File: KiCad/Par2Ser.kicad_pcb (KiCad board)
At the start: 2 copper layers, 47 x 50 mm, 31 parts, among them J1 DB25_Male, J2 USB_C_Receptacle_USB2.0, U1 LC4032V-5TN48C, U3 FT240XS-R

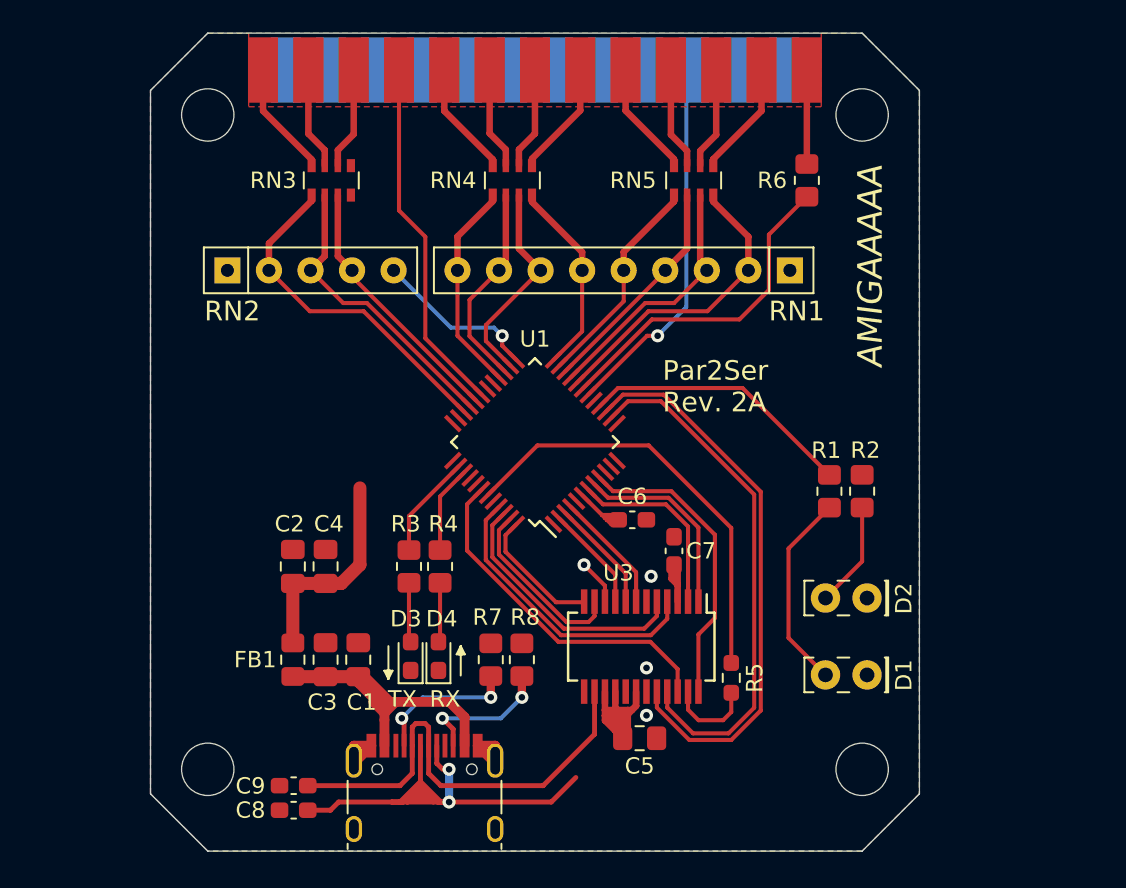
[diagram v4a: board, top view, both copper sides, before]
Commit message: Add resistors on the two USB data lines
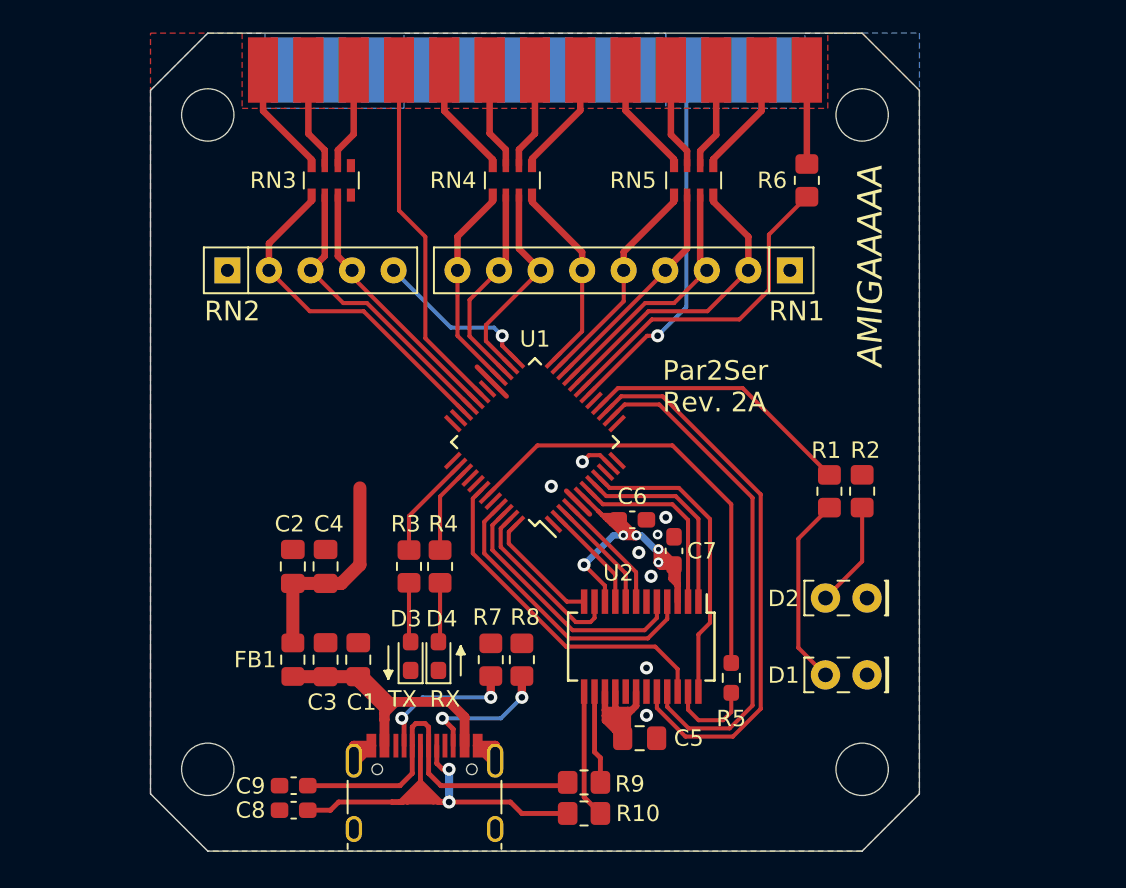
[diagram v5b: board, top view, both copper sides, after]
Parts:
- added R10: 27, Resistor_SMD:R_0805_2012Metric_Pad1.20x1.40mm_HandSolder, F.Cu at (150.5, 132.7)
- added R9: 27, Resistor_SMD:R_0805_2012Metric_Pad1.20x1.40mm_HandSolder, F.Cu at (150.5, 130.8)
- renumbered U3 to U2
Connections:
- U2 pad 13: USBDP -> Net-(R10-Pad1)
- U2 pad 14: USBDM -> Net-(R9-Pad1)
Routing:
- net 3V3: track 31.0 -> 49.1 mm, vias 1 -> 5
- net Net-(R10-Pad1): track 0.00 -> 7.86 mm
- net Net-(R9-Pad1): track 0.00 -> 5.70 mm
- net USBDM: track 27.9 -> 22.4 mm
- net GND: track 6.87 -> 11.4 mm, vias 3 -> 7
- net TCK: track 0.00 -> 2.22 mm, vias 0 -> 1
- net RXF: track 32.2 -> 31.3 mm
- net CLK12M: track 26.5 -> 27.4 mm
- net USBDP: track 35.9 -> 35.1 mm
- net WR: track 8.04 -> 7.45 mm

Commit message: Move to four layers
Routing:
- net TCK: track 2.22 -> 25.4 mm
- net TDI: track 0.00 -> 23.1 mm, vias 0 -> 1
- net TD0: track 0.00 -> 16.0 mm
- net TMS: track 10.1 -> 24.4 mm
- net 3V3: track 49.1 -> 62.1 mm, vias 5 -> 9
- added copper zone on 3V3.Cu, net 3V3
- added copper zone on GND.Cu, net GND
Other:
- copper layers 2 -> 4
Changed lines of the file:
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@@
     (thickness 1.6)
     (drawings 31)
-    (tracks 378)
+    (tracks 407)
     (zones 0)
     (modules 33)
@@
   (layers
     (0 F.Cu signal)
+    (1 GND.Cu power)
+    (2 3V3.Cu power)
     (31 B.Cu signal)
     (32 B.Adhes user)
@@
   )
   (setup
-    (last_trace_width 0.25)
+    (last_trace_width 0.5)
     (user_trace_width 0.1524)
     (user_trace_width 0.1778)
@@
   (gr_line (start 171 88.5) (end 171 131.5) (layer Edge.Cuts) (width 0.05))
   (gr_line (start 127.5 85) (end 167.5 85) (layer Edge.Cuts) (width 0.05))
+  (via (at 168.8 112) (size 0.8) (drill 0.4) (layers F.Cu B.Cu) (net 16))
+  (via (at 148.05 113.4) (size 0.8) (drill 0.4) (layers F.Cu B.Cu) (net 32))
   (via (at 154.3177 123.8) (size 0.8) (drill 0.4) (layers F.Cu B.Cu) (net 1))
   (segment (start 136.43 128.555) (end 136.43 129.47) (width 0.6) (layer F.Cu) (net 1))
@@
   (segment (start 136.43 129.47) (end 136.585 129.47) (width 0.6) (layer F.Cu) (net 1))
   (via (at 154.3177 126.7) (size 0.8) (drill 0.4) (layers F.Cu B.Cu) (net 1))
-  (via (at 154.6 118.2) (size 0.8) (drill 0.4) (layers F.Cu B.Cu) (net 1))
+  (via (at 154.6 118.3) (size 0.8) (drill 0.4) (layers F.Cu B.Cu) (net 1))
   (via (at 155.5 114.6) (size 0.8) (drill 0.4) (layers F.Cu B.Cu) (net 1))
   (via (at 153.85 116.75) (size 0.8) (drill 0.4) (layers F.Cu B.Cu) (net 1))
   (via (at 155 115.65) (size 0.6) (drill 0.3) (layers F.Cu B.Cu) (net 1))
-  (via (at 148.5 112.7) (size 0.8) (drill 0.4) (layers F.Cu B.Cu) (net 1))
+  (via (at 149 112.55) (size 0.8) (drill 0.4) (layers F.Cu B.Cu) (net 1))
   (segment (start 145.760661 107.2) (end 143.960661 105.4) (width 0.3) (layer F.Cu) (net 1))
   (segment (start 149.419669 112.980331) (end 150.85 114.410662) (width 0.3) (layer F.Cu) (net 1))
+  (via (at 167.5 110.8) (size 0.8) (drill 0.4) (layers F.Cu B.Cu) (net 16))
   (segment (start 157.195 88.330666) (end 157.195 87.254) (width 0.381) (layer B.Cu) (net 2))
   (segment (start 150.752691 107.100862) (end 154.353553 103.5) (width 0.25) (layer F.Cu) (net 2))
@@
   (segment (start 152.3 115.7) (end 150.5 117.5) (width 0.4) (layer B.Cu) (net 16))
   (segment (start 152.9 115.7) (end 152.3 115.7) (width 0.4) (layer B.Cu) (net 16))
+  (segment (start 167.5 110.8) (end 167.5 112) (width 0.5) (layer F.Cu) (net 16))
+  (segment (start 167.5 110.8) (end 167.6 110.8) (width 0.5) (layer F.Cu) (net 16))
+  (segment (start 168.8 112) (end 167.5 112) (width 0.5) (layer F.Cu) (net 16))
+  (segment (start 167.9 111.1) (end 167.9 111.6) (width 0.5) (layer F.Cu) (net 16))
+  (segment (start 167.9 111.6) (end 167.5 112) (width 0.5) (layer F.Cu) (net 16))
+  (segment (start 167.6 110.8) (end 167.9 111.1) (width 0.5) (layer F.Cu) (net 16))
+  (segment (start 167.9 111.1) (end 168.8 112) (width 0.5) (layer F.Cu) (net 16))
+  (via (at 152.3 129.5) (size 0.8) (drill 0.4) (layers F.Cu B.Cu) (net 16))
+  (via (at 153.4 129.5) (size 0.8) (drill 0.4) (layers F.Cu B.Cu) (net 16))
+  (segment (start 152.3 129.5) (end 153.4 129.5) (width 0.8) (layer F.Cu) (net 16))
+  (segment (start 152.8625 128.9375) (end 152.3 129.5) (width 0.8) (layer F.Cu) (net 16))
+  (segment (start 152.8625 128.1) (end 152.8625 128.9375) (width 0.8) (layer F.Cu) (net 16))
+  (segment (start 152.8625 128.9625) (end 153.4 129.5) (width 0.8) (layer F.Cu) (net 16))
+  (segment (start 152.8625 128.1) (end 152.8625 128.9625) (width 0.8) (layer F.Cu) (net 16))
+  (segment (start 152.3 128.6625) (end 152.8625 128.1) (width 0.5) (layer F.Cu) (net 16))
+  (segment (start 152.3 129.5) (end 152.3 128.6625) (width 0.5) (layer F.Cu) (net 16))
+  (segment (start 153.4 128.6375) (end 152.8625 128.1) (width 0.5) (layer F.Cu) (net 16))
+  (segment (start 153.4 129.5) (end 153.4 128.6375) (width 0.5) (layer F.Cu) (net 16))
   (segment (start 132.7 118.6375) (end 132.7 122.275) (width 0.8) (layer F.Cu) (net 21))
   (segment (start 132.7 118.6375) (end 134.7 118.6375) (width 0.8) (layer F.Cu) (net 21))
@@
   (segment (start 145.42 126.88) (end 146.7 125.6) (width 0.25) (layer B.Cu) (net 31))
   (segment (start 141.84 126.88) (end 145.42 126.88) (width 0.25) (layer B.Cu) (net 31))
+  (segment (start 148.05 114.439087) (end 148.631371 115.020458) (width 0.25) (layer F.Cu) (net 32))
+  (segment (start 148.05 113.4) (end 148.05 114.439087) (width 0.25) (layer F.Cu) (net 32))
+  (segment (start 148.05 113.4) (end 126.8 113.4) (width 0.25) (layer B.Cu) (net 32))
   (via (at 150.4 111.2) (size 0.8) (drill 0.4) (layers F.Cu B.Cu) (net 33))
   (segment (start 151.481982 110.800001) (end 152.166905 111.484924) (width 0.25) (layer F.Cu) (net 33))
   (segment (start 150.799999 110.800001) (end 151.481982 110.800001) (width 0.25) (layer F.Cu) (net 33))
   (segment (start 150.4 111.2) (end 150.799999 110.800001) (width 0.25) (layer F.Cu) (net 33))
+  (segment (start 150.4 111.2) (end 127.2 111.2) (width 0.3) (layer B.Cu) (net 33))
   (via (at 145.5 103.5) (size 0.8) (drill 0.4) (layers F.Cu B.Cu) (net 34))
   (segment (start 145.5 104.110913) (end 146.368629 104.979542) (width 0.25) (layer F.Cu) (net 34))
@@
   (segment (start 142.36 103) (end 145 103) (width 0.25) (layer B.Cu) (net 34))
   (segment (start 138.86 99.5) (end 142.36 103) (width 0.25) (layer B.Cu) (net 34))
+  (segment (start 138.86 99.5) (end 132.46 105.9) (width 0.25) (layer B.Cu) (net 34))
+  (segment (start 132.46 105.9) (end 127.2 105.9) (width 0.25) (layer B.Cu) (net 34))
+  (segment (start 142.833095 108.515076) (end 142.118019 107.8) (width 0.25) (layer F.Cu) (net 35))
+  (segment (start 142.118019 107.8) (end 127.15 107.8) (width 0.25) (layer F.Cu) (net 35))
   (segment (start 157.4925 114.6925) (end 157.4925 119.75) (width 0.25) (layer F.Cu) (net 36))
   (segment (start 156.1 113.3) (end 157.4925 114.6925) (width 0.25) (layer F.Cu) (net 36))
@@
       )
     )
+  )
+  (zone (net 1) (net_name GND) (layer GND.Cu) (hatch edge 0.508)
+    (connect_pads (clearance 0.2032))
+    (min_thickness 0.2032)
+    (fill yes (arc_segments 32) (thermal_gap 0.2032) (thermal_bridge_width 0.508))
+    (polygon
+      (pts
+        (xy 124 88.5) (xy 127.5 85) (xy 167.5 85) (xy 171 88.5) (xy 171 135)
+        (xy 127.5 135) (xy 124 131.5)
+      )
+    )
+  )
+  (zone (net 16) (net_name 3V3) (layer 3V3.Cu) (hatch edge 0.508)
+    (connect_pads (clearance 0.2032))
+    (min_thickness 0.2032)
+    (fill yes (arc_segments 32) (thermal_gap 0.2032) (thermal_bridge_width 0.508))
+    (polygon
+      (pts
+        (xy 124 88.5) (xy 127.5 85) (xy 167.5 85) (xy 171 88.5) (xy 171 131.5)
+        (xy 167.5 135) (xy 124 135)
+      )
+    )

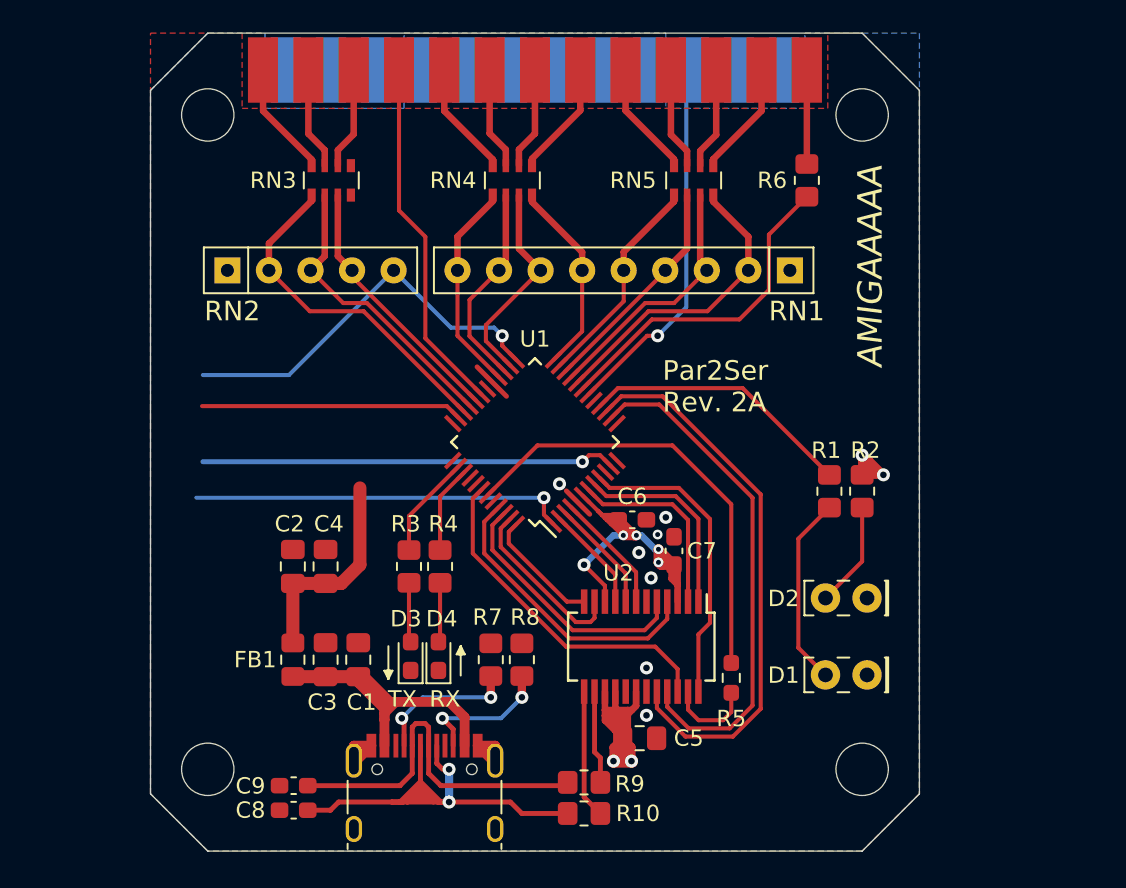
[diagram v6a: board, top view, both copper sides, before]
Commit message: Add remaining caps on 3V3 pins for CPLD and route power traces
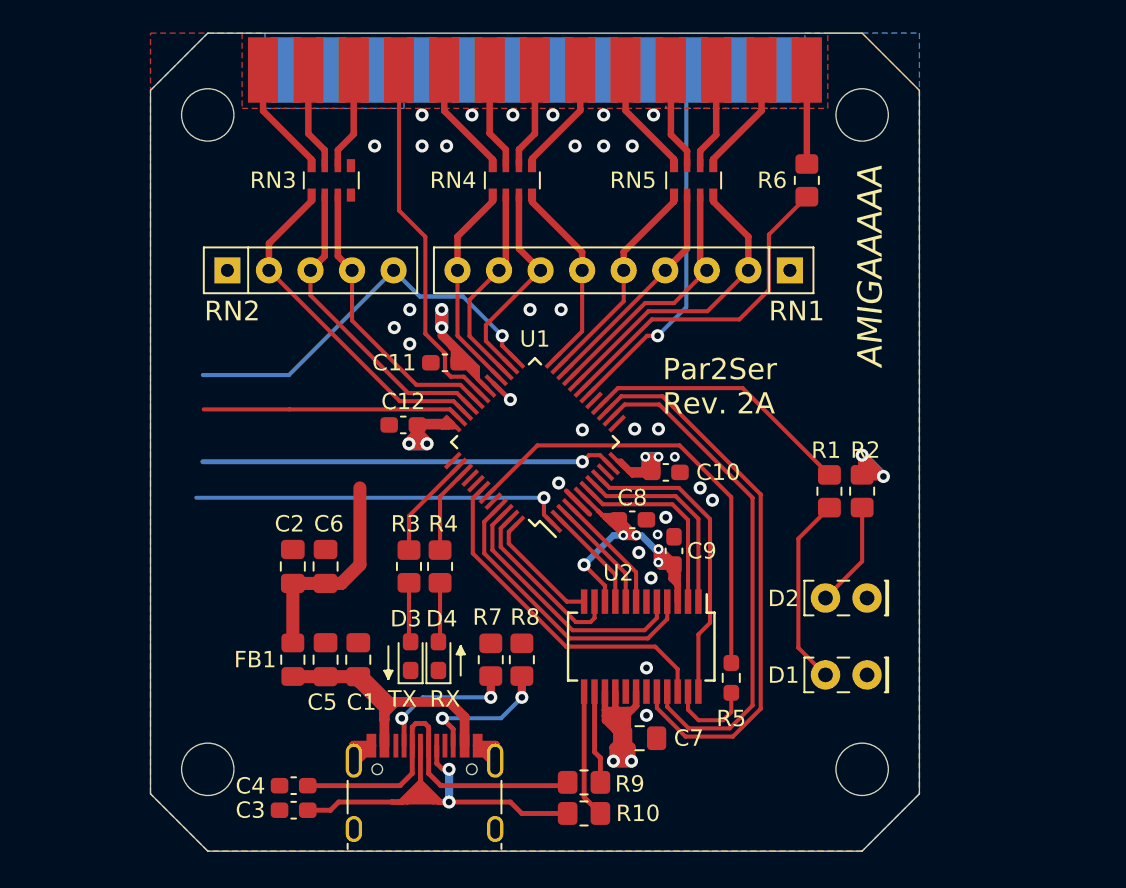
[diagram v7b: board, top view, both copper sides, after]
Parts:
- removed the C6 at (153.4, 114.8)
- added C10: 0.1uF, Capacitor_SMD:C_0603_1608Metric_Pad1.08x0.95mm_HandSolder, F.Cu at (155.5, 111.8)
- added C11: 0.1uF, Capacitor_SMD:C_0603_1608Metric_Pad1.08x0.95mm_HandSolder, F.Cu at (142.0, 105.2)
- added C12: 0.1uF, Capacitor_SMD:C_0603_1608Metric_Pad1.08x0.95mm_HandSolder, F.Cu at (139.4, 109.0)
- added C8: 0.1uF, Capacitor_SMD:C_0603_1608Metric_Pad1.08x0.95mm_HandSolder, F.Cu at (153.4, 114.8)
- renumbered C8 to C3, C9 to C4, C3 to C5, C4 to C6, C5 to C7, C7 to C9
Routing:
- net 3V3: track 62.1 -> 107.2 mm, vias 9 -> 15
- net BUSY_B9: track 16.1 -> 17.6 mm
- net POUT_B10: track 18.2 -> 19.1 mm
- net GND: track 11.4 -> 10.6 mm, vias 7 -> 31
